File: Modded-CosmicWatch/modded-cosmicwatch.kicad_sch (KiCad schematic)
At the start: 5 parts, among them SW1 SW_Push

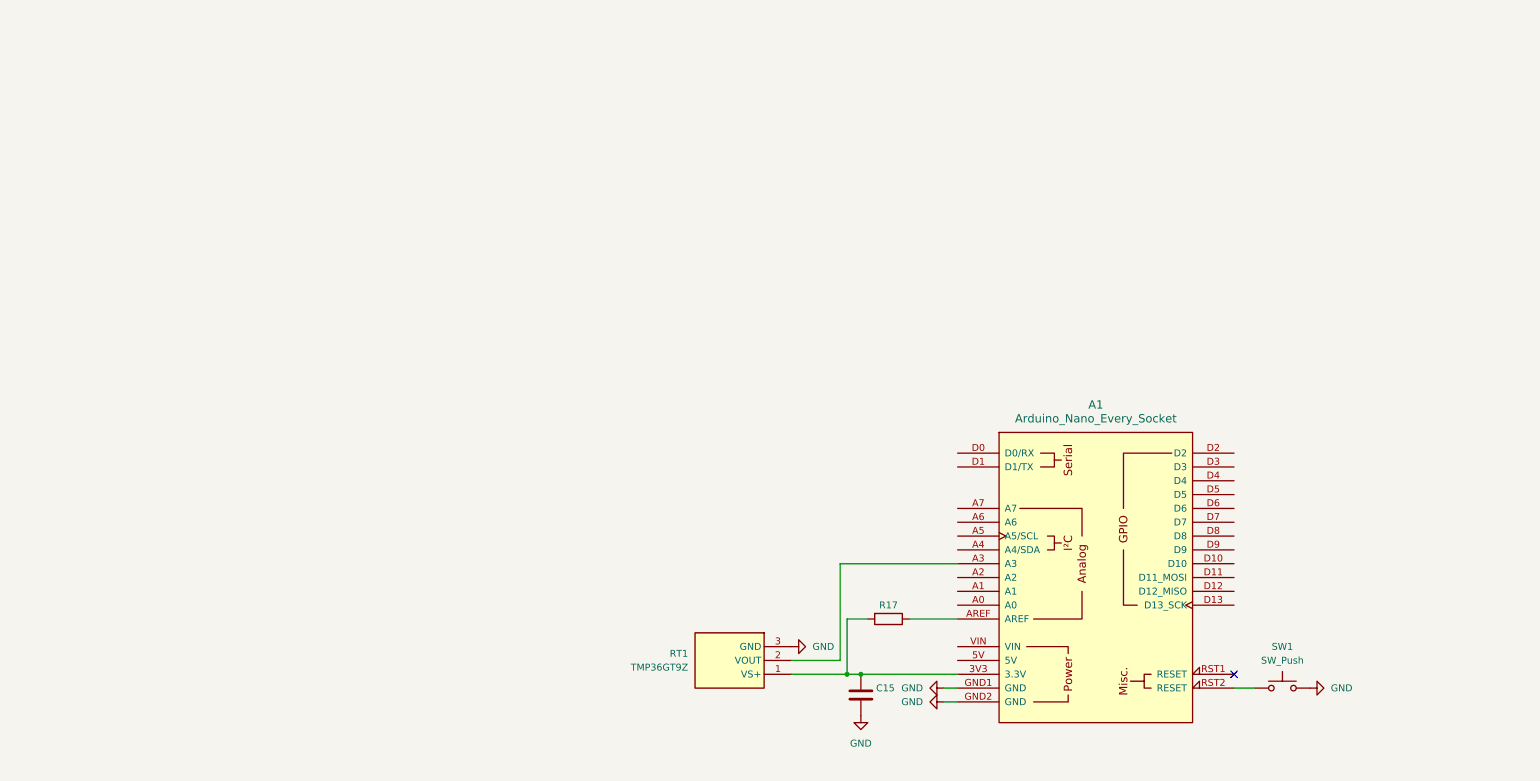
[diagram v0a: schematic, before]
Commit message: finished traces for acs and generated gerber files
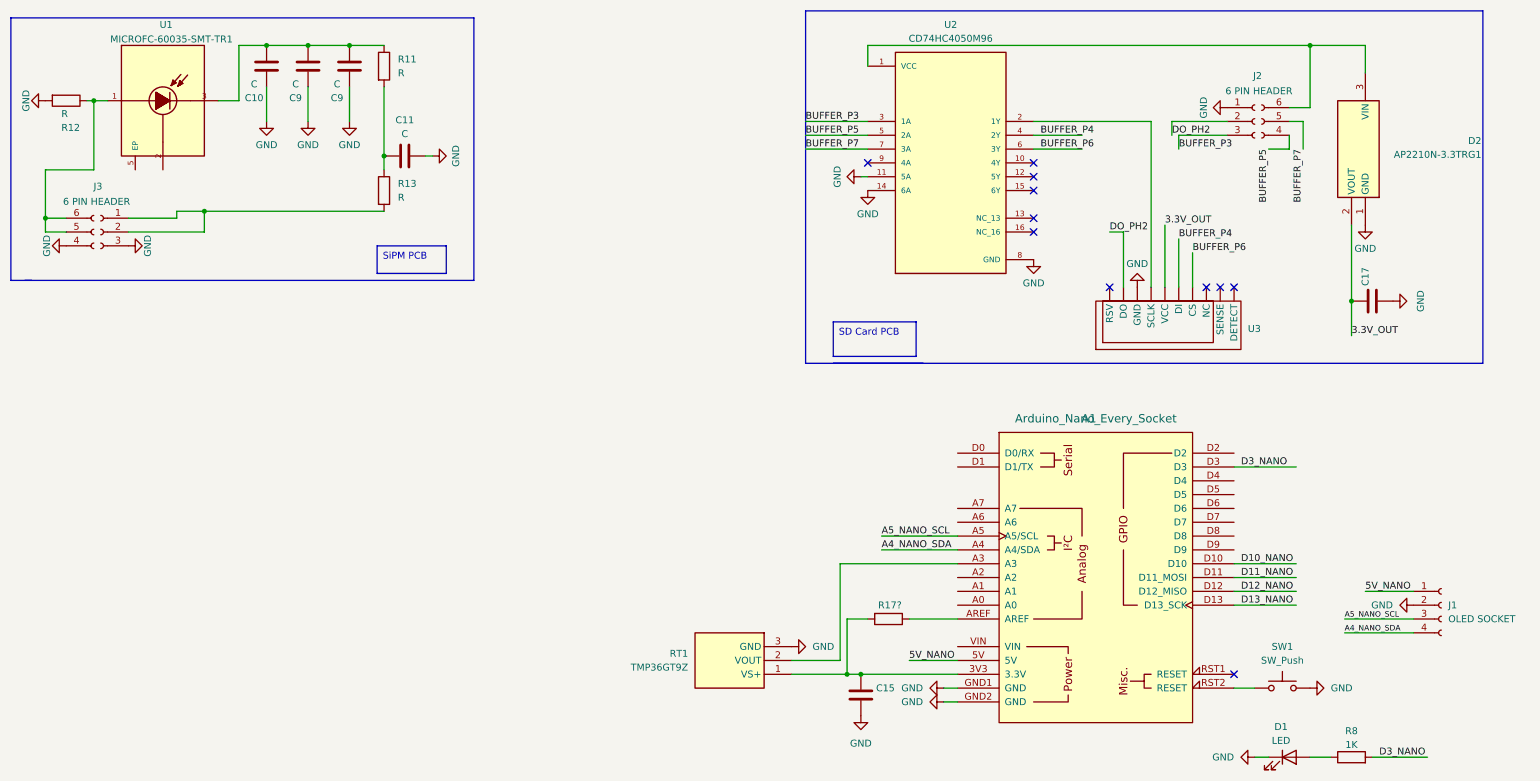
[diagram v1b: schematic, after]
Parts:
- added C10, C11, C17, C9 (x2): C, symbol Device:C
- added D1: LED, symbol Device:LED
- added D2: AP2210N-3.3TRG1, SOT95P282X145-3N, symbol AP2210N-3_3TRG1:AP2210N-3.3TRG1
- added J1: OLED SOCKET, symbol Connector:Conn_01x04_Socket
- added J2, J3: 6 PIN HEADER, symbol Connector:Conn_01x06_Socket
- added R11, R12, R13: R, symbol Device:R
- added R8: 1K, symbol Device:R
- added U1: MICROFC-60035-SMT-TR1, MICROFC-60035-SMT-TR1:XDCR_MICROFC-60035-SMT-TR1, symbol MICROFC-60035-SMT-TR1:MICROFC-60035-SMT-TR1
- added U2: CD74HC4050M96, CD74HC4050M96:SOIC127P600X175-16N, symbol CD74HC4050M96:CD74HC4050M96
- added U3: ~, symbol microsdslot:uxcell_MicroSD_Card_Slot
- renumbered R17 to R17?
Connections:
- net GND: now also C10.1, C11.1, C17.2, C9.1, C9.1, D1.1 (K), D2.1 (GND), J1.2 (Pin_2), J2.1 (Pin_1), J3.3 (Pin_3), J3.4 (Pin_4), R12.2, U2.11 (5A), U2.14 (6A), U2.8 (GND), U3. (VCC)
- net 5V_NANO: now reaches A1.5V
- net 5V_NANO: now also J1.1 (Pin_1)
- net A4_NANO_SDA: now reaches A1.A4 (A4/SDA)
- net A4_NANO_SDA: now also J1.4 (Pin_4)
- net A5_NANO_SCL: now reaches A1.A5 (A5/SCL)
- net A5_NANO_SCL: now also J1.3 (Pin_3)
- net D10_NANO: now reaches A1.D10
- net D11_NANO: now reaches A1.D11 (D11_MOSI)
- net D12_NANO: now reaches A1.D12 (D12_MISO)
- net D13_NANO: now reaches A1.D13 (D13_SCK)
- net D3_NANO: now reaches A1.D3
- net D3_NANO: now also R8.2
- new net: D2.3 (VIN), J2.6 (Pin_6), U2.1 (VCC)
- new net: J3.5 (Pin_5), J3.6 (Pin_6), R12.1, U1.1
- new net: C10.2, C9.2, C9.2, R11.1, U1.3
- new net: D1.2 (A), R8.1
- new net: C11.2, R11.2, R13.1
- new net: J3.1 (Pin_1), J3.2 (Pin_2), R13.2
- new net: U2.2 (1Y), U3. (VCC)
- new net 3.3V_OUT: C17.1, D2.2 (VOUT), U3. (VCC)
- new net BUFFER_P3: J2.3 (Pin_3), U2.3 (1A)
- new net BUFFER_P4: U2.4 (2Y), U3. (VCC)
- new net BUFFER_P5: J2.4 (Pin_4), U2.5 (2A)
- new net BUFFER_P6: U2.6 (3Y), U3. (VCC)
- new net BUFFER_P7: J2.5 (Pin_5), U2.7 (3A)
- new net DO_PH2: J2.2 (Pin_2), U3. (VCC)
- no-connect marks 1 -> 11
